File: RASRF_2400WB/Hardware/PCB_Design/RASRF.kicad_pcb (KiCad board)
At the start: 4 copper layers, 77.6 x 56.8 mm, 172 parts, among them J1 PCIexpress_x8, J3 60312202111527, J4 Conn_01x04_Pin, U1 LD1117S18TR_SOT223, U2 STM32C031G6Ux, U3 SN74AXC4T774RSVR, U4 TCR2EF285, U5 MAX2831ETM+T, U6 HHM1902B1, U7 ADC3221IRGZR, Y1 7L-40.000MBS-T, Y2 ABM10-166-12.000MHZ-T3

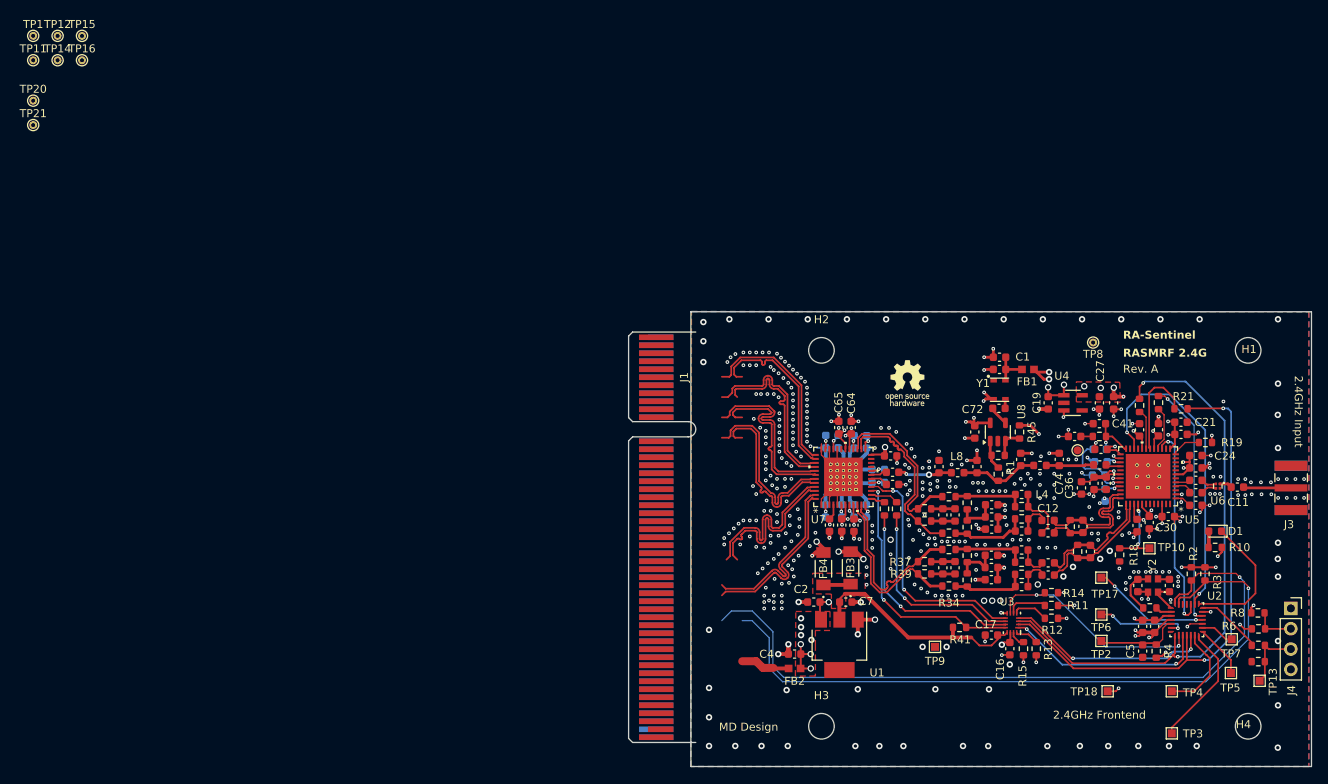
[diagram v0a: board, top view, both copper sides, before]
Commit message: Corrected the RASRF_2400WB PCB design files. They where not the latest from Rev. A. sent to manufacturer.
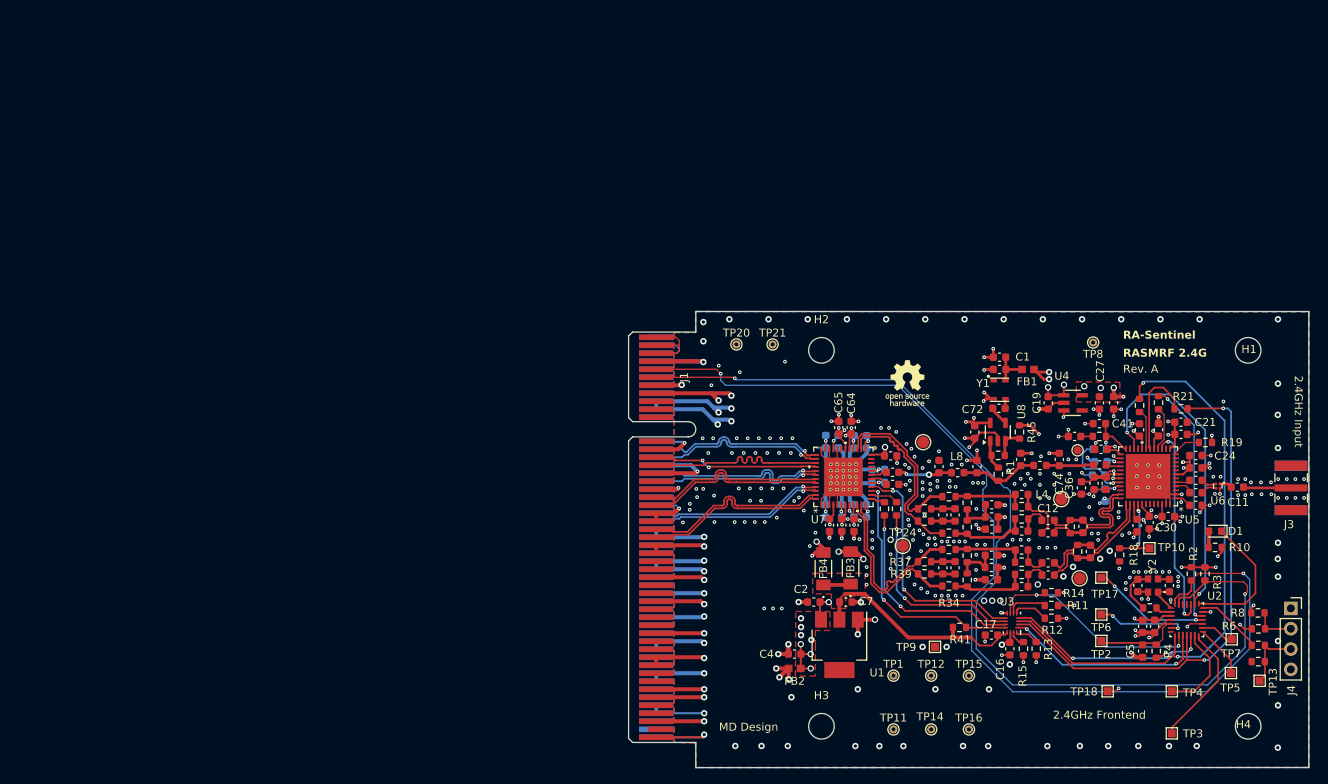
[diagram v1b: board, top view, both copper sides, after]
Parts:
- added TP22: TestPoint, TestPoint:TestPoint_Pad_D1.5mm, F.Cu at (131.8, 68.8)
- added TP23: TestPoint, TestPoint:TestPoint_Pad_D1.5mm, F.Cu at (112.3, 51.8)
- added TP24: TestPoint, TestPoint:TestPoint_Pad_D1.5mm, F.Cu at (109.7, 64.8)
- added TP25: TestPoint, TestPoint:TestPoint_Pad_D1.5mm, F.Cu at (129.5, 58.9)
- moved TP16 138.9 mm to (118.0, 87.7)
- moved TP14 137.6 mm to (113.3, 87.7)
- moved TP15 136.7 mm to (118.0, 81.0)
- moved TP11 136.2 mm to (108.6, 87.7)
- moved TP12 135.4 mm to (113.3, 81.0)
- moved TP1 134.0 mm to (108.6, 81.0)
- moved TP21 96.4 mm to (93.5, 39.6)
- moved TP20 93.0 mm to (88.9, 39.6)
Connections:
- J1 pad A13: /DCLK_P -> /DB1_P
- J1 pad A14: /DCLK_N -> /DB1_N
- J1 pad A16: /DA0_P -> /FCLK_P
- J1 pad A17: /DA0_N -> /FCLK_N
- J1 pad A21: /DA1_N -> /DA1_P
- J1 pad A22: /DA1_P -> /DA1_N
- J1 pad A25: /DB0_P -> unconnected-(J1-PERp2-PadA25)
- J1 pad A26: /DB0_N -> unconnected-(J1-PERn2-PadA26)
- J1 pad A29: /DB1_P -> unconnected-(J1-PERp3-PadA29)
- J1 pad A30: /DB1_N -> unconnected-(J1-PERn3-PadA30)
- J1 pad A35: /FCLK_P -> unconnected-(J1-PERp4-PadA35)
- J1 pad A36: /FCLK_N -> unconnected-(J1-PERn4-PadA36)
- J1 pad B14: unconnected-(J1-PETp0-PadB14) -> /DB0_N
- J1 pad B15: unconnected-(J1-PETn0-PadB15) -> /DB0_P
- J1 pad B19: unconnected-(J1-PETp1-PadB19) -> /DCLK_P
- J1 pad B20: unconnected-(J1-PETn1-PadB20) -> /DCLK_N
- J1 pad B23: unconnected-(J1-PETp2-PadB23) -> /DA0_P
- J1 pad B24: unconnected-(J1-PETn2-PadB24) -> /DA0_N
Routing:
- net GND: track 120.7 -> 302.6 mm, vias 418 -> 337
- net /I2C_SDA: track 87.8 -> 127.0 mm, vias 1 -> 2
- net /I2C_SCL: track 93.0 -> 131.8 mm, vias 1 -> 2
- net /3V3_IN: track 6.18 -> 37.9 mm, vias 0 -> 9
- net Net-(J1-+12V-PadB1): track 0.00 -> 10.2 mm
- net Net-(J1-+12V-PadA2): track 0.00 -> 6.34 mm
- net /DA0_N: track 21.8 -> 23.5 mm
- net /DA0_P: track 21.8 -> 23.5 mm
- net /DB0_N: track 22.1 -> 20.6 mm, vias 0 -> 2
- net /FCLK_N: track 22.7 -> 22.1 mm, vias 0 -> 1
- net /FCLK_P: track 22.7 -> 22.1 mm, vias 0 -> 1
- net /DA1_N: track 22.1 -> 21.7 mm, vias 0 -> 1
- net /DA1_P: track 22.1 -> 21.7 mm, vias 0 -> 1
- net /DB1_N: track 22.6 -> 22.1 mm, vias 0 -> 1
- net /DB1_P: track 22.5 -> 22.1 mm, vias 0 -> 1
- removed copper zone on In2.Cu, net GND
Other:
- board size 77.6 x 56.8 mm -> 76.6 x 57 mm
